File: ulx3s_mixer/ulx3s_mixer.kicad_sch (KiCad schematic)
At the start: 47 parts, among them J1 Conn_02x20_Odd_Even, J2 Conn_Coaxial, Q1 BC846, U1 MAX2606, U2 ADEX-10L+, U3 VAM-6+, U4 PL133-27

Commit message: Added all part numbers
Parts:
- C1, C11, C2, C3, C5, C7: footprint Resistor_SMD:R_0603_1608Metric -> Capacitor_SMD:C_0603_1608Metric
- C10, C4: footprint Resistor_SMD:R_0603_1608Metric -> Capacitor_SMD:C_0603_1608Metric; MPN (none) -> 885382206001
- C12, C9: MPN (none) -> C0603C104K8RACTU
- C13, C6: MPN (none) -> HH18N102J500CT
- C14, C8: MPN (none) -> CL32A106KOJNNNE
- C15: MPN (none) -> RF18N270J500CT
- J1, L1, L2, R1, R2: MPN (none) -> DNP
- J2: MPN (none) -> CONSMA020.062-G
- L6: MPN (none) -> AISC-1210-R33J-T
- R10, R11, R12, R13, R4, R5, R6, R9: MPN (none) -> 0603WAJ0103T5E
- R3: MPN (none) -> RMCF0603JT270R
- R7: value 92R -> 100R; MPN (none) -> CR0603-JW-101ELF
- R8: MPN (none) -> RC0603FR-10510RL
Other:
- title: (none) -> ULX3S Mixer + 1-bit ADC PCB
- moved on the sheet: C1, C10, C11, C12, C13, C14, C15, C2, C3, C4, C5, C6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

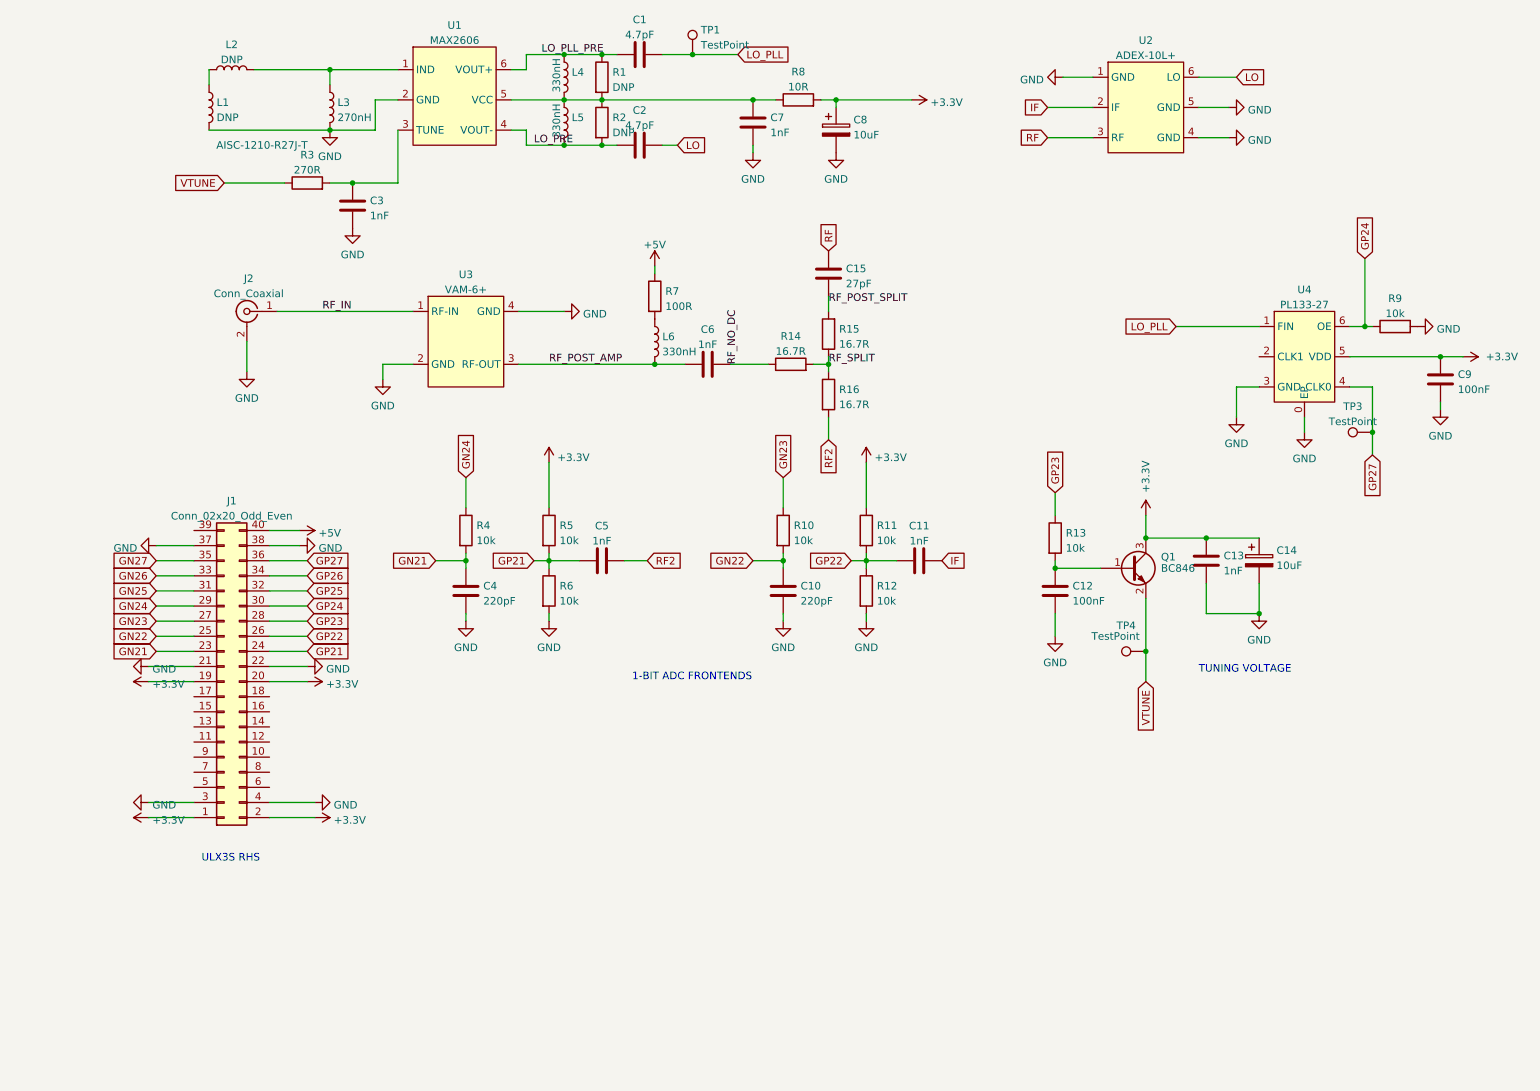
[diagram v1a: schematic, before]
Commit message: Added CS4344 to schematic
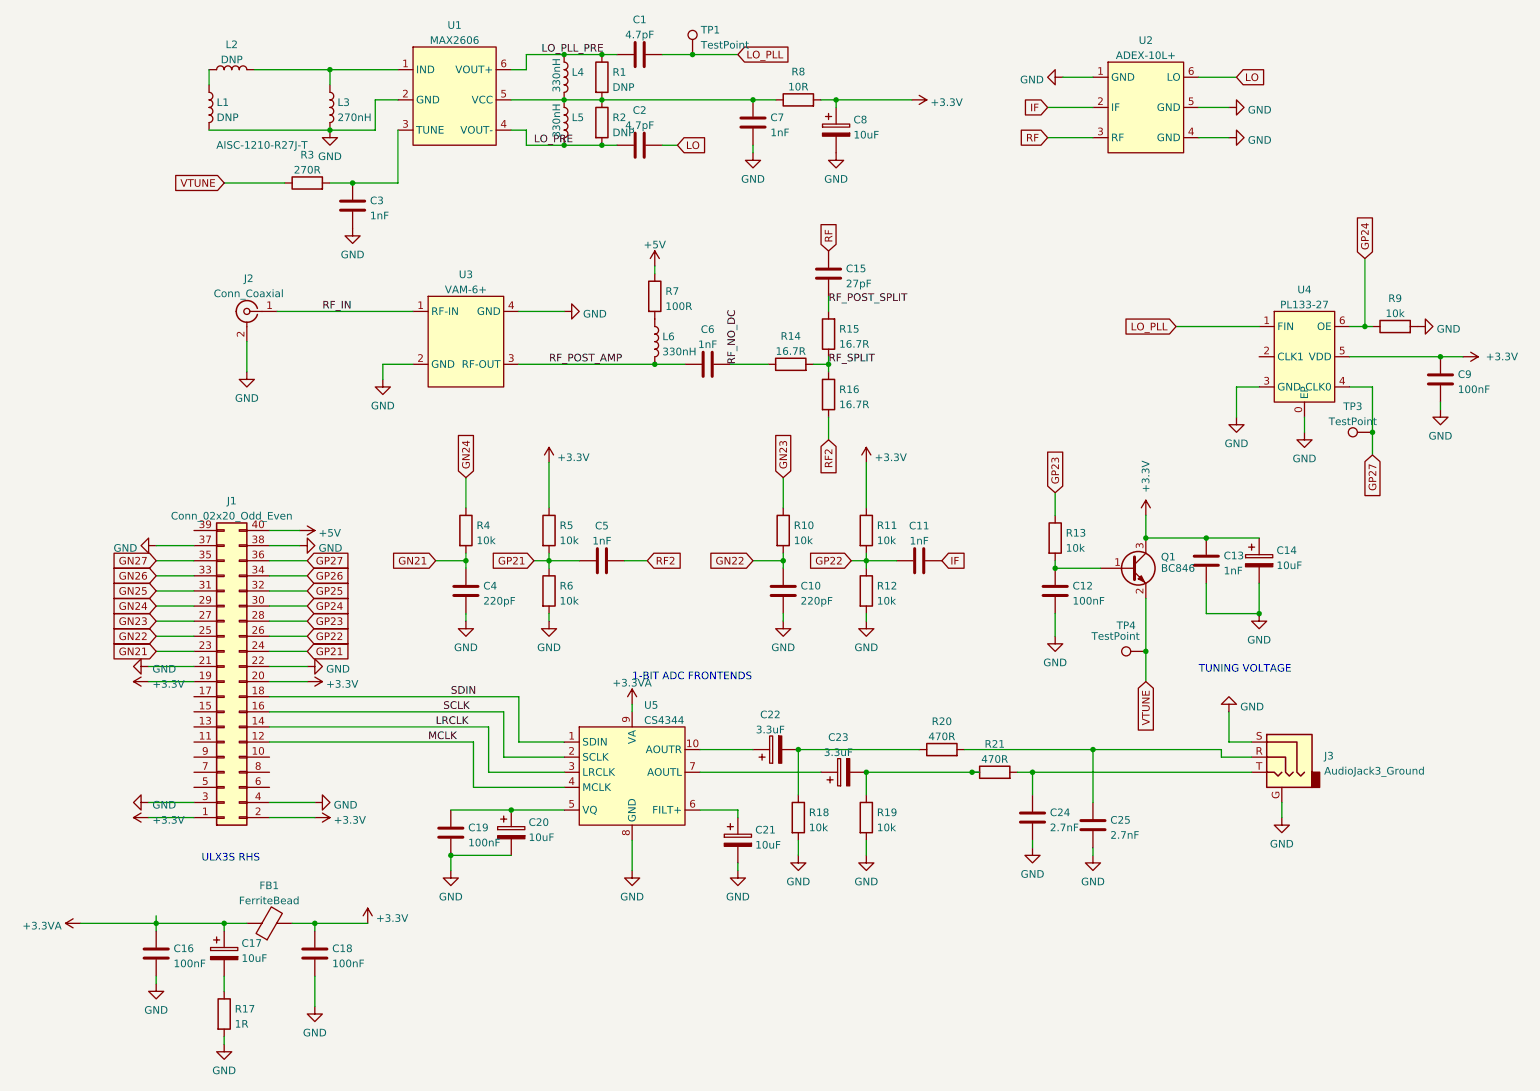
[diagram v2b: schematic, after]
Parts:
- added C16, C18, C19: 100nF, Capacitor_SMD:C_0603_1608Metric, symbol Device:C
- added C17, C20, C21: 10uF, Capacitor_SMD:C_1210_3225Metric, symbol Device:C_Polarized
- added C22, C23: 3.3uF, Capacitor_SMD:C_1210_3225Metric, symbol Device:C_Polarized
- added C24, C25: 2.7nF, Capacitor_SMD:C_0603_1608Metric, symbol Device:C
- added FB1: FerriteBead, symbol Device:FerriteBead
- added J3: AudioJack3_Ground, symbol Connector:AudioJack3_Ground
- added R17: 1R, Resistor_SMD:R_0603_1608Metric, symbol Device:R
- added R18, R19: 10k, Resistor_SMD:R_0603_1608Metric, symbol Device:R
- added R20, R21: 470R, Resistor_SMD:R_0603_1608Metric, symbol Device:R
- added U5: CS4344, symbol mixer:CS4344
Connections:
- net +3V3: now also C18.1, FB1.2
- net GND: now also C16.2, C18.2, C19.2, C20.2, C21.2, C24.1, C25.1, J3.G, J3.S, R17.2, R18.2, R19.2, U5.8 (GND)
- net MCLK: now reaches J1.12 (Pin_12)
- net MCLK: now also U5.4 (MCLK)
- net LRCLK: now reaches J1.14 (Pin_14)
- net LRCLK: now also U5.3 (LRCLK)
- net SCLK: now reaches J1.16 (Pin_16)
- net SCLK: now also U5.2 (SCLK)
- net SDIN: now reaches J1.18 (Pin_18)
- net SDIN: now also U5.1 (SDIN)
- new net: C17.2, R17.1
- new net: C23.2, R19.1, R21.1
- new net: C24.2, J3.T, R21.2
- new net: C23.1, U5.7 (AOUTL)
- new net: C22.2, R18.1, R20.1
- new net: C25.2, J3.R, R20.2
- new net: C21.1, U5.6 (FILT+)
- new net: C19.1, C20.1, U5.5 (VQ)
- new net: C22.1, U5.10 (AOUTR)
- new net +3.3VA: C16.1, C17.1, FB1.1, U5.9 (VA)

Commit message: Finished design, exported BOM + gerbers
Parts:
- C22, C23: MPN (none) -> CL31B335KOHNNNE
- C24, C25: MPN (none) -> 0603B272K500CT
- FB1: footprint (none) -> Inductor_SMD:L_0402_1005Metric; MPN (none) -> MMZ1005S601CT000
- J3: footprint (none) -> Connector_Audio:Jack_3.5mm_CUI_SJ-3523-SMT_Horizontal; MPN (none) -> SJ-3523-SMT-TR
- R17: MPN (none) -> WR06W1R00FTL
- R20: MPN (none) -> 652-CR0603JW-471ELF
- R21: MPN 0603WAJ0103T5E -> 652-CR0603JW-471ELF
- U5: footprint (none) -> Package_SO:TSSOP-10_3x3mm_P0.5mm; MPN (none) -> CS4344-CZZR
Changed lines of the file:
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@@
     (property "Reference" "FB1" (id 0) (at 60.9092 162.5686 90))
     (property "Value" "FerriteBead" (id 1) (at 60.9092 165.1055 90))
-    (property "Footprint" "" (id 2) (at 60.96 170.688 90)
+    (property "Footprint" "Inductor_SMD:L_0402_1005Metric" (id 2) (at 60.96 170.688 90)
       (effects (font (size 1.27 1.27)) hide)
     )
     (property "Datasheet" "~" (id 3) (at 60.96 168.91 0)
+      (effects (font (size 1.27 1.27)) hide)
+    )
+    (property "MPN" "MMZ1005S601CT000 " (id 4) (at 60.96 168.91 0)
       (effects (font (size 1.27 1.27)) hide)
     )
@@
       (effects (font (size 1.27 1.27)) hide)
     )
-    (property "MPN" "" (id 4) (at 53.34 184.15 0)
+    (property "MPN" "WR06W1R00FTL" (id 4) (at 53.34 184.15 0)
       (effects (font (size 1.27 1.27)) hide)
     )
@@
       (effects (font (size 1.27 1.27)) hide)
     )
-    (property "MPN" "0603WAJ0103T5E" (id 4) (at 182.88 143.51 0)
+    (property "MPN" "652-CR0603JW-471ELF" (id 4) (at 182.88 143.51 0)
       (effects (font (size 1.27 1.27)) hide)
     )
@@
       (effects (font (size 1.27 1.27)) hide)
     )
-    (property "MPN" "" (id 4) (at 157.48 143.51 0)
+    (property "MPN" "CL31B335KOHNNNE" (id 4) (at 157.48 143.51 0)
       (effects (font (size 1.27 1.27)) hide)
     )
@@
       (effects (font (size 1.27 1.27)) hide)
     )
-    (property "MPN" "" (id 4) (at 173.99 139.7 0)
+    (property "MPN" "652-CR0603JW-471ELF" (id 4) (at 173.99 139.7 0)
       (effects (font (size 1.27 1.27)) hide)
     )
@@
       (effects (font (size 1.27 1.27)) hide)
     )
-    (property "MPN" "" (id 4) (at 189.23 151.13 0)
+    (property "MPN" "0603B272K500CT" (id 4) (at 189.23 151.13 0)
       (effects (font (size 1.27 1.27)) hide)
     )
@@
       (effects (font (size 1.27 1.27)) hide)
     )
-    (property "MPN" "" (id 4) (at 199.39 152.4 0)
+    (property "MPN" "0603B272K500CT" (id 4) (at 199.39 152.4 0)
       (effects (font (size 1.27 1.27)) hide)
     )
@@
       (effects (font (size 1.27 1.27)) (justify left))
     )
-    (property "Footprint" "" (id 2) (at 119.38 143.51 0)
+    (property "Footprint" "Package_SO:TSSOP-10_3x3mm_P0.5mm" (id 2) (at 119.38 143.51 0)
       (effects (font (size 1.27 1.27)) hide)
     )
     (property "Datasheet" "" (id 3) (at 119.38 143.51 0)
+      (effects (font (size 1.27 1.27)) hide)
+    )
+    (property "MPN" "CS4344-CZZR" (id 4) (at 121.92 143.51 0)
       (effects (font (size 1.27 1.27)) hide)
     )
@@
       (effects (font (size 1.27 1.27)) (justify right))
     )
-    (property "Footprint" "" (id 2) (at 231.14 140.97 0)
+    (property "Footprint" "Connector_Audio:Jack_3.5mm_CUI_SJ-3523-SMT_Horizontal" (id 2) (at 231.14 140.97 0)
       (effects (font (size 1.27 1.27)) hide)
     )
     (property "Datasheet" "~" (id 3) (at 231.14 140.97 0)
+      (effects (font (size 1.27 1.27)) hide)
+    )
+    (property "MPN" "SJ-3523-SMT-TR " (id 4) (at 231.14 140.97 0)
       (effects (font (size 1.27 1.27)) hide)
     )
@@
       (effects (font (size 1.27 1.27)) hide)
     )
-    (property "MPN" "" (id 4) (at 146.05 139.7 0)
+    (property "MPN" "CL31B335KOHNNNE" (id 4) (at 146.05 139.7 0)
       (effects (font (size 1.27 1.27)) hide)
     )
@@
     )
     (path "/07183797-56ce-440e-8b7c-3ff509466165"
-      (reference "FB1") (unit 1) (value "FerriteBead") (footprint "")
+      (reference "FB1") (unit 1) (value "FerriteBead") (footprint "Inductor_SMD:L_0402_1005Metric")
     )
     (path "/33594662-1c2f-44ee-8074-0ef091e0fe1b"
@@
     )
     (path "/d3cf9aab-ed47-44a0-bc84-eeaf88780847"
-      (reference "J3") (unit 1) (value "AudioJack3_Ground") (footprint "")
+      (reference "J3") (unit 1) (value "AudioJack3_Ground") (footprint "Connector_Audio:Jack_3.5mm_CUI_SJ-3523-SMT_Horizontal")
     )
     (path "/2f4638c6-65df-40c0-ad8f-3b71ca158ae0"
@@
     )
     (path "/c019b44d-3f59-43d5-85a1-f1b9aa9dcccc"
-      (reference "U5") (unit 1) (value "CS4344") (footprint "")
-    )
-  )
+      (reference "U5") (unit 1) (value "CS4344") (footprint "Package_SO:TSSOP-10_3x3mm_P0.5mm")
+    )
+  )
